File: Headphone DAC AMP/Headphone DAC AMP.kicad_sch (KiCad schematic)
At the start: 2 parts, among them J3 SJ-3502-SMT

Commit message: Litterally didnt add anything because I spent an hour trying to understand how impedance matching works
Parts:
- added R10, R8, R9: 10, Resistor_SMD:R_0805_2012Metric_Pad1.20x1.40mm_HandSolder, symbol Device:R
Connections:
- net Clocking/MCLK_DAC: now also R10.1
- net DAC/BCK: now also R9.2
- net DAC/WS: now also R8.2
- new net DAC/MCLK: R10.2
- new net USB Audio Input/BCLK: R9.1
- new net USB Audio Input/LRCLK: R8.1
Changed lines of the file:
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@@
 	(wire
 		(pts
-			(xy 90.17 76.2) (xy 143.51 76.2)
+			(xy 90.17 76.2) (xy 125.73 76.2)
 		)
 		(stroke
@@
 	(wire
 		(pts
-			(xy 90.17 73.66) (xy 143.51 73.66)
+			(xy 90.17 73.66) (xy 111.76 73.66)
 		)
 		(stroke
@@
 	(wire
 		(pts
-			(xy 114.3 71.12) (xy 143.51 71.12)
+			(xy 114.3 71.12) (xy 120.65 71.12)
 		)
 		(stroke
@@
 	(wire
 		(pts
+			(xy 133.35 76.2) (xy 143.51 76.2)
+		)
+		(stroke
+			(width 0)
+			(type default)
+		)
+	)
+	(wire
+		(pts
 			(xy 90.17 148.59) (xy 100.33 148.59)
 		)
@@
 	(wire
 		(pts
+			(xy 119.38 73.66) (xy 143.51 73.66)
+		)
+		(stroke
+			(width 0)
+			(type default)
+		)
+	)
+	(wire
+		(pts
 			(xy 90.17 85.09) (xy 143.51 85.09)
+		)
+		(stroke
+			(width 0)
+			(type default)
+		)
+	)
+	(wire
+		(pts
+			(xy 128.27 71.12) (xy 143.51 71.12)
 		)
 		(stroke
@@
 	)
 	(symbol
+		(lib_id "Device:R")
+		(at 129.54 76.2 90)
+		(unit 1)
+		(exclude_from_sim no)
+		(in_bom yes)
+		(on_board yes)
+		(dnp no)
+		(fields_autoplaced yes)
+		(property "Reference" "R8"
+			(at 129.54 69.85 90)
+			(effects
+				(font
+					(size 1.27 1.27)
+				)
+			)
+		)
+		(property "Value" "10"
+			(at 129.54 72.39 90)
+			(effects
+				(font
+					(size 1.27 1.27)
+				)
+			)
+		)
+		(property "Footprint" "Resistor_SMD:R_0805_2012Metric_Pad1.20x1.40mm_HandSolder"
+			(at 129.54 77.978 90)
+			(effects
+				(font
+					(size 1.27 1.27)
+				)
+				(hide yes)
+			)
+		)
+		(property "Datasheet" "~"
+			(at 129.54 76.2 0)
+			(effects
+				(font
+					(size 1.27 1.27)
+				)
+				(hide yes)
+			)
+		)
+		(property "Description" "Resistor"
+			(at 129.54 76.2 0)
+			(effects
+				(font
+					(size 1.27 1.27)
+				)
+				(hide yes)
+			)
+		)
+		(pin "1"
+		)
+		(pin "2"
+		)
+		(instances
+			(project "Headphone DAC AMP"
+				(path "/d034eddd-efbc-47be-a25c-37cbfbab4cd8"
+					(reference "R8")
+					(unit 1)
+				)
+			)
+		)
+	)
+	(symbol
 		(lib_id "power:GND")
 		(at 74.93 170.18 0)
@@
 	)
 	(symbol
+		(lib_id "Device:R")
+		(at 115.57 73.66 90)
+		(unit 1)
+		(exclude_from_sim no)
+		(in_bom yes)
+		(on_board yes)
+		(dnp no)
+		(fields_autoplaced yes)
+		(property "Reference" "R9"
+			(at 115.57 67.31 90)
+			(effects
+				(font
+					(size 1.27 1.27)
+				)
+			)
+		)
+		(property "Value" "10"
+			(at 115.57 69.85 90)
+			(effects
+				(font
+					(size 1.27 1.27)
+				)
+			)
+		)
+		(property "Footprint" "Resistor_SMD:R_0805_2012Metric_Pad1.20x1.40mm_HandSolder"
+			(at 115.57 75.438 90)
+			(effects
+				(font
+					(size 1.27 1.27)
+				)
+				(hide yes)
+			)
+		)
+		(property "Datasheet" "~"
+			(at 115.57 73.66 0)
+			(effects
+				(font
+					(size 1.27 1.27)
+				)
+				(hide yes)
+			)
+		)
+		(property "Description" "Resistor"
+			(at 115.57 73.66 0)
+			(effects
+				(font
+					(size 1.27 1.27)
+				)
+				(hide yes)
+			)
+		)
+		(pin "1"
+		)
+		(pin "2"
+		)
+		(instances
+			(project "Headphone DAC AMP"
+				(path "/d034eddd-efbc-47be-a25c-37cbfbab4cd8"
+					(reference "R9")
+					(unit 1)
+				)
+			)
+		)
+	)
+	(symbol
 		(lib_id "power:GND")
 		(at 203.2 93.98 0)
@@
 					(unit 1)
 				)
+			)
+		)
+	)
+	(symbol
+		(lib_id "Device:R")
+		(at 124.46 71.12 90)
+		(unit 1)
+		(exclude_from_sim no)
+		(in_bom yes)
+		(on_board yes)
+		(dnp no)
+		(fields_autoplaced yes)
+		(property "Reference" "R10"
+			(at 124.46 64.77 90)
+			(effects
+				(font
+					(size 1.27 1.27)
+				)
+			)
+		)
+		(property "Value" "10"
+			(at 124.46 67.31 90)
+			(effects
+				(font
+					(size 1.27 1.27)
+				)
+			)
+		)
+		(property "Footprint" "Resistor_SMD:R_0805_2012Metric_Pad1.20x1.40mm_HandSolder"
+			(at 124.46 72.898 90)
+			(effects
+				(font
+					(size 1.27 1.27)
+				)
+				(hide yes)
+			)
+		)
+		(property "Datasheet" "~"
+			(at 124.46 71.12 0)
+			(effects
+				(font
+					(size 1.27 1.27)
+				)
+				(hide yes)
+			)
+		)
+		(property "Description" "Resistor"
+			(at 124.46 71.12 0)
+			(effects
+				(font
+					(size 1.27 1.27)
+				)
+				(hide yes)
+			)
+		)
+		(pin "1"
+		)
+		(pin "2"
+		)
+		(instances
+			(project "Headphone DAC AMP"
+				(path "/d034eddd-efbc-47be-a25c-37cbfbab4cd8"
+					(reference "R10")
+					(unit 1)
+				)

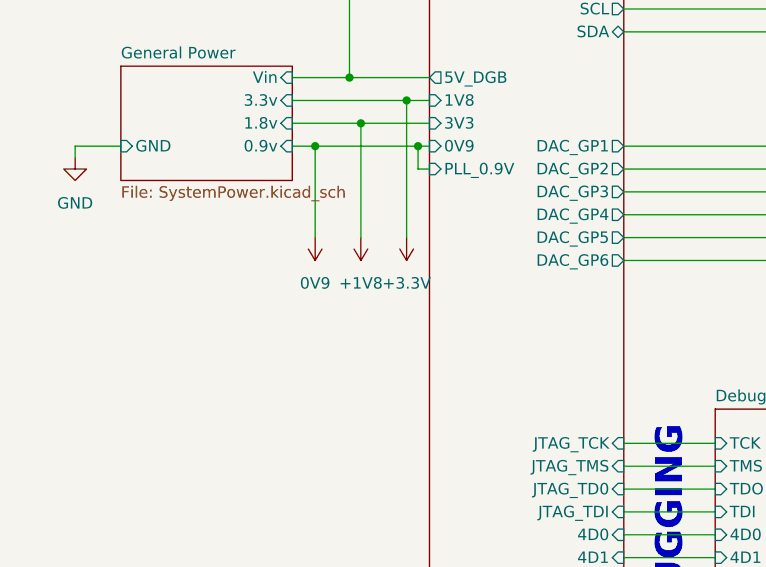
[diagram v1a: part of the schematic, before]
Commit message: Finisshed routing debug and added some power planes
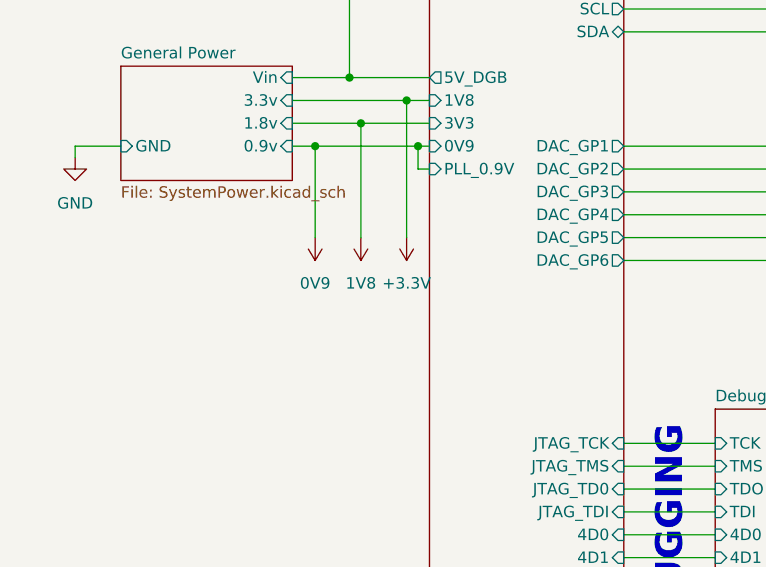
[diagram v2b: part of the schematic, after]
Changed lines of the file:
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@@
 			)
 		)
-		(property "Value" "+1V8"
+		(property "Value" "1V8"
 			(at 60.96 115.57 0)
 			(effects

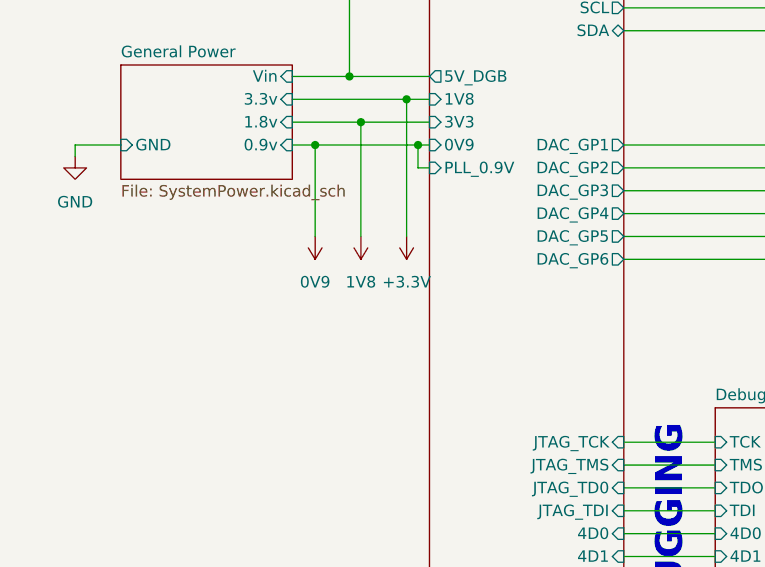
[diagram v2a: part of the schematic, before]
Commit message: almost done with XMOS, DAC still needed
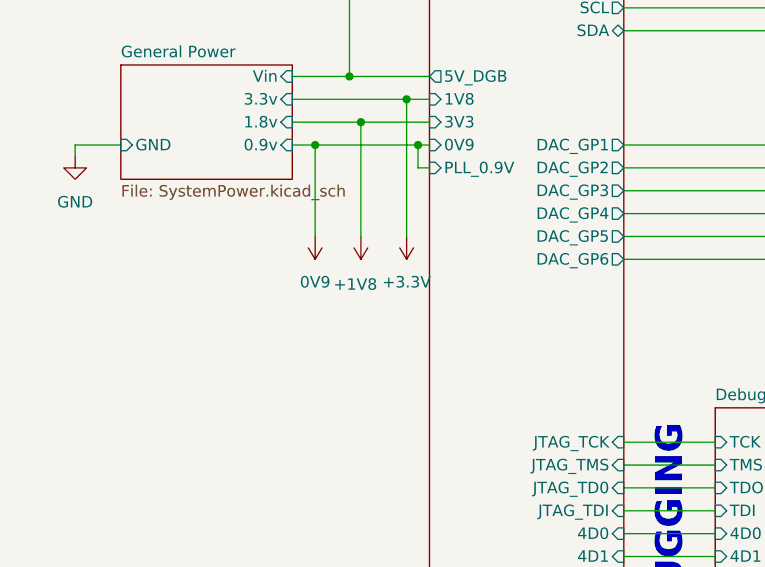
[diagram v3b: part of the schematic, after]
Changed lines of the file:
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@@
 		(on_board yes)
 		(dnp no)
-		(fields_autoplaced yes)
 		(property "Reference" "#PWR0106"
 			(at 60.96 106.68 0)
@@
 			)
 		)
-		(property "Value" "1V8"
-			(at 60.96 115.57 0)
+		(property "Value" "+1V8"
+			(at 57.912 115.824 0)
 			(effects
 				(font
 					(size 1.27 1.27)
 				)
+				(justify right)
 			)
 		)

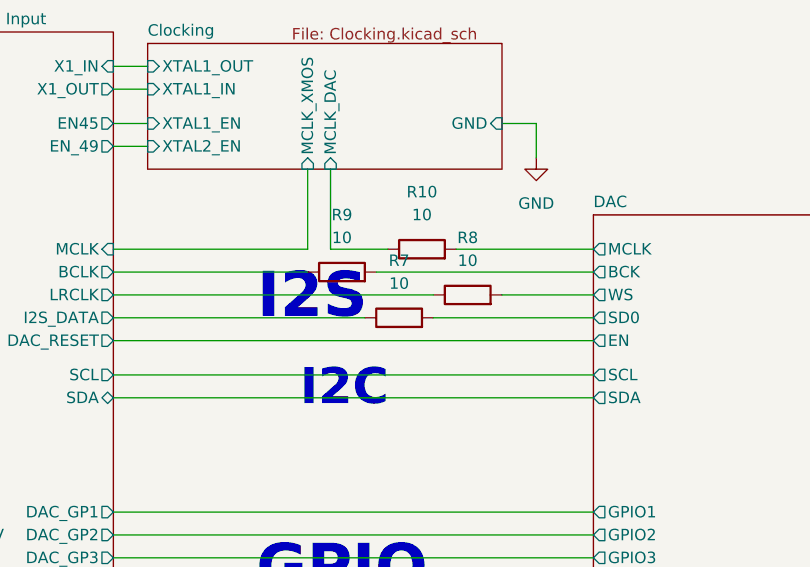
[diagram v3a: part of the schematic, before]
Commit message: (Post Board Order) updated BOM with component links
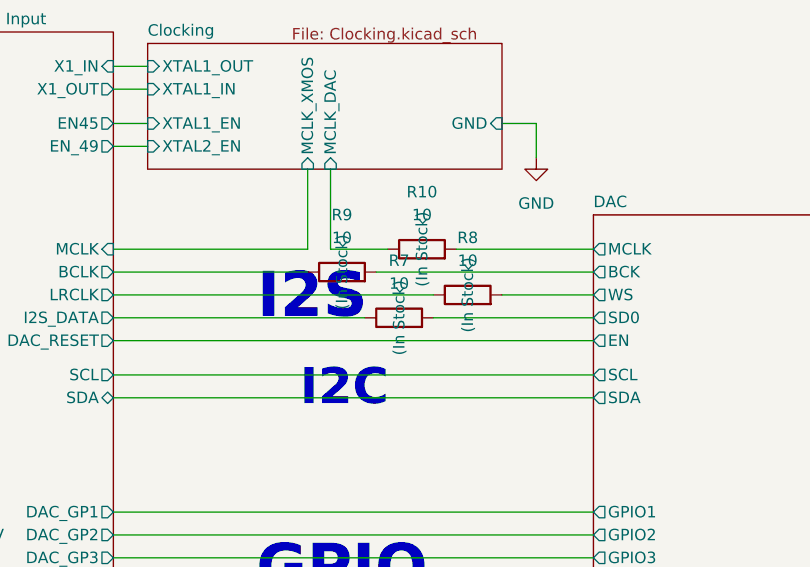
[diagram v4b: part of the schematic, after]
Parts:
- R10, R7, R8, R9: CUI_PURCHASE_URL (none) -> (In Stock)
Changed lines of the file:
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@@
+			)
+		)
+		(property "CUI_PURCHASE_URL" "(In Stock)"
+			(at 121.92 78.74 0)
+			(effects
+				(font
+					(size 1.27 1.27)
+				)
 			)
 		)
@@
 			)
 		)
+		(property "CUI_PURCHASE_URL" "(In Stock)"
+			(at 129.54 76.2 0)
+			(effects
+				(font
+					(size 1.27 1.27)
+				)
+			)
+		)
 		(pin "1"
 		)
@@
 			)
 		)
+		(property "CUI_PURCHASE_URL" "(In Stock)"
+			(at 115.57 73.66 0)
+			(effects
+				(font
+					(size 1.27 1.27)
+				)
+			)
+		)
 		(pin "1"
 		)
@@
 			)
 		)
+		(property "CUI_PURCHASE_URL" "(In Stock)"
+			(at 124.46 71.12 0)
+			(effects
+				(font
+					(size 1.27 1.27)
+				)
+			)
+		)

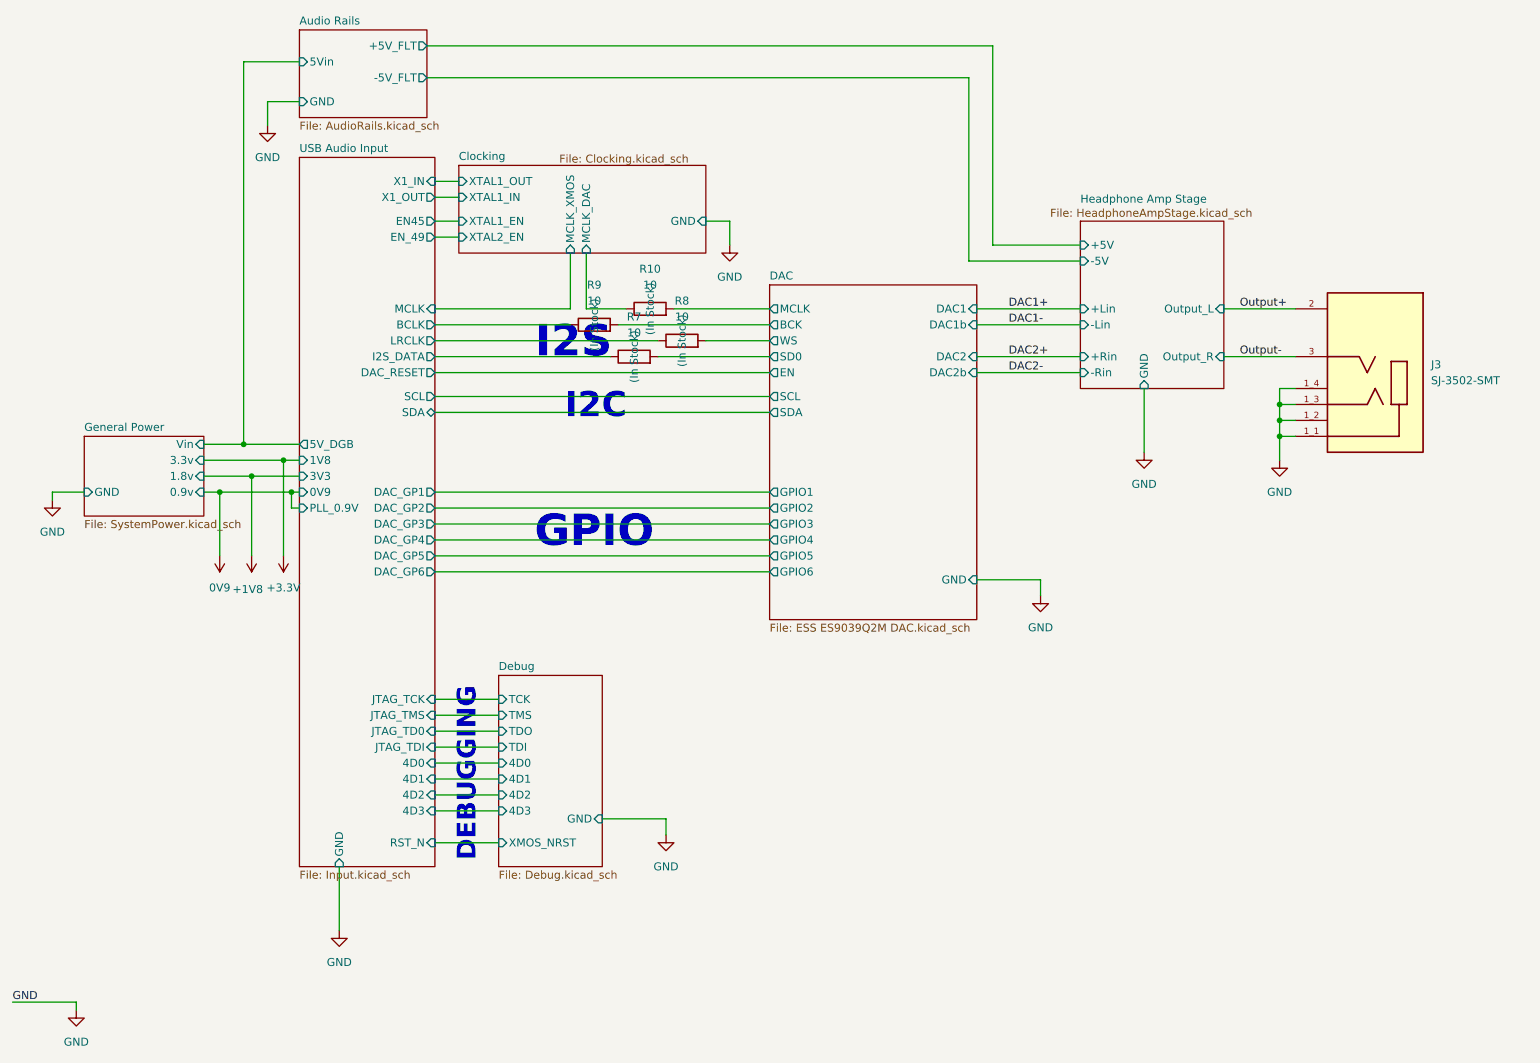
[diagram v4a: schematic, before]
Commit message: Removed DAC Components
Removed all analog components and increased vias to 0.3mm
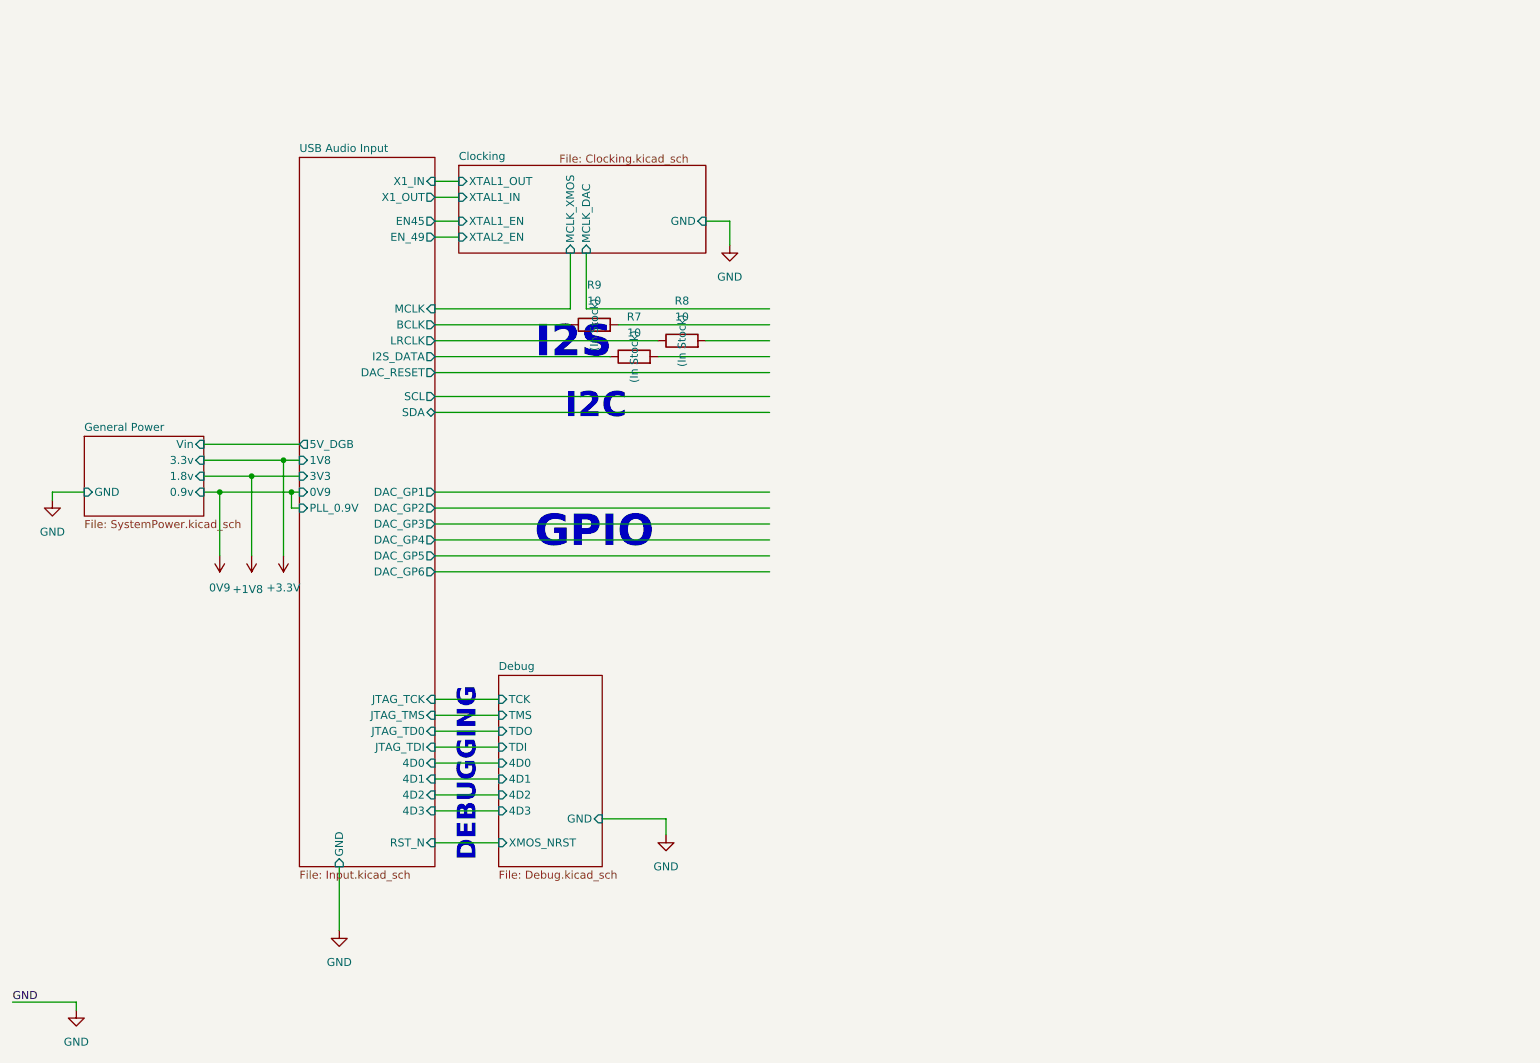
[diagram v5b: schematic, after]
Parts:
- removed J3: SJ-3502-SMT, SJ_3502_SMT_TR:CUI_SJ-3502-SMT, symbol SJ-3502-SMT:SJ-3502-SMT
- removed R10: 10, Resistor_SMD:R_0805_2012Metric_Pad1.20x1.40mm_HandSolder, symbol Device:R
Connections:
- net DAC/BCK: no longer names the net of R9.2
- net DAC/SD0: no longer names the net of R7.2
- net DAC/WS: no longer names the net of R8.2
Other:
- removed sheet Audio Rails
- removed sheet DAC
- removed sheet Headphone Amp Stage

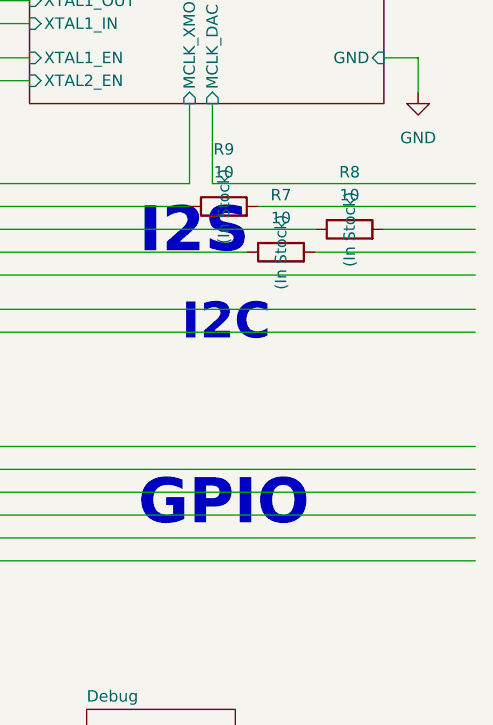
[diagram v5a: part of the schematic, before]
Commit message: Update PCB layout and net assignments for new connector
Added M50-3551042 connector footprint (J2) and updated net assignments for I2S, I2C, and GPIO signals. Relocated and rotated several components (R7, R9, R13, R18, R19, D3, D4, C99) to accommodate layout changes. Updated netlist to remove unused nets and assign correct signal names. Modified backup files accordingly.
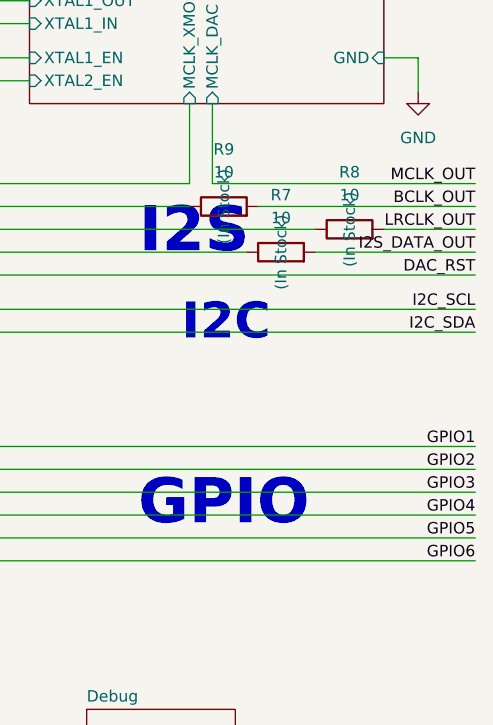
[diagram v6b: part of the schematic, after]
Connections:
- net I2S_DATA_OUT: now reaches R7.2
- net LRCLK_OUT: now reaches R8.2
- net BCLK_OUT: now reaches R9.2
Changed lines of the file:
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@@
+		)
+	)
+	(label "GPIO4"
+		(at 143.51 107.95 180)
+		(effects
+			(font
+				(size 1.27 1.27)
+			)
+			(justify right bottom)
+		)
+	)
+	(label "GPIO2"
+		(at 143.51 102.87 180)
+		(effects
+			(font
+				(size 1.27 1.27)
+			)
+			(justify right bottom)
+		)
+	)
+	(label "LRCLK_OUT"
+		(at 143.51 76.2 180)
+		(effects
+			(font
+				(size 1.27 1.27)
+			)
+			(justify right bottom)
+		)
+	)
+	(label "BCLK_OUT"
+		(at 143.51 73.66 180)
+		(effects
+			(font
+				(size 1.27 1.27)
+			)
+			(justify right bottom)
+		)
+	)
+	(label "MCLK_OUT"
+		(at 143.51 71.12 180)
+		(effects
+			(font
+				(size 1.27 1.27)
+			)
+			(justify right bottom)
+		)
+	)
+	(label "I2C_SCL"
+		(at 143.51 85.09 180)
+		(effects
+			(font
+				(size 1.27 1.27)
+			)
+			(justify right bottom)
+		)
+	)
+	(label "I2S_DATA_OUT"
+		(at 143.51 78.74 180)
+		(effects
+			(font
+				(size 1.27 1.27)
+			)
+			(justify right bottom)
+		)
+	)
+	(label "GPIO5"
+		(at 143.51 110.49 180)
+		(effects
+			(font
+				(size 1.27 1.27)
+			)
+			(justify right bottom)
+		)
+	)
+	(label "I2C_SDA"
+		(at 143.51 87.63 180)
+		(effects
+			(font
+				(size 1.27 1.27)
+			)
+			(justify right bottom)
+		)
+	)
+	(label "GPIO1"
+		(at 143.51 100.33 180)
+		(effects
+			(font
+				(size 1.27 1.27)
+			)
+			(justify right bottom)
+		)
+	)
+	(label "DAC_RST"
+		(at 143.51 81.28 180)
+		(effects
+			(font
+				(size 1.27 1.27)
+			)
+			(justify right bottom)
+		)
+	)
+	(label "GPIO6"
+		(at 143.51 113.03 180)
+		(effects
+			(font
+				(size 1.27 1.27)
+			)
+			(justify right bottom)
 		)
 	)
@@
 		)
 	)
+	(label "GPIO3"
+		(at 143.51 105.41 180)
+		(effects
+			(font
+				(size 1.27 1.27)
+			)
+			(justify right bottom)
+		)
+	)
